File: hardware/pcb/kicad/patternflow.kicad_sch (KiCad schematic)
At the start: 11 parts, among them J1 Conn_02x08_Odd_Even, J3 Screw_Terminal_01x02, SW1 RotaryEncoder_Switch, SW2 RotaryEncoder_Switch, SW3 RotaryEncoder_Switch, SW4 RotaryEncoder_Switch, U1 ESP32-S3-DevKit-44pin

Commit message: hardware(pcb): v3.0 test board — hybrid power input (USB-C + 2-pin screw terminal)
Per the plan in issue #114: instead of splitting into two PCBs, one board now
carries both power-input options.

- Add a 2-pin screw terminal footprint on the back as a beginner-friendly
  bypass for the difficult USB-C THT soldering (strip a USB cable, screw it in)
- Clean up routing
- Bump silkscreen version text to v3.0
- Bake v3.0 test Gerbers (DRC clean: 0 violations, 0 unconnected) into
  hardware/pcb/gerber/experiment/ with a do-not-order README
- Delete patternflow_v2.2_test_gerber.zip so nobody orders the superseded
  test revision by mistake; BUILD_GUIDE warning updated to match

Co-Authored-By: Claude Opus 4.8 <noreply@anthropic.com>
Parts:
- added J4: Screw_Terminal_01x02, TerminalBlock:TerminalBlock_MaiXu_MX126-5.0-02P_1x02_P5.00mm, symbol Connector:Screw_Terminal_01x02
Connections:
- net +5V: now also J4.2 (Pin_2)
- net GND: now also J4.1 (Pin_1)
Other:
- title: PatternFlow -> Patternflow

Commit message: fix(pcb): correct C11 value typo 1000uF/1.6V -> 1000uF/16V
The part is a 16V Rubycon PX (16PX1000MEFC10X12.5); the schematic
value read 1.6V, which would be under-spec on the 5V rail.

Co-Authored-By: Claude Fable 5 <noreply@anthropic.com>
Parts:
- C11: value 1000uF/1.6V -> 1000uF/16V
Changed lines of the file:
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@@
 			)
 		)
-		(property "Value" "1000uF/1.6V"
+		(property "Value" "1000uF/16V"
 			(at 94.361 109.22 90)
 			(show_name no)

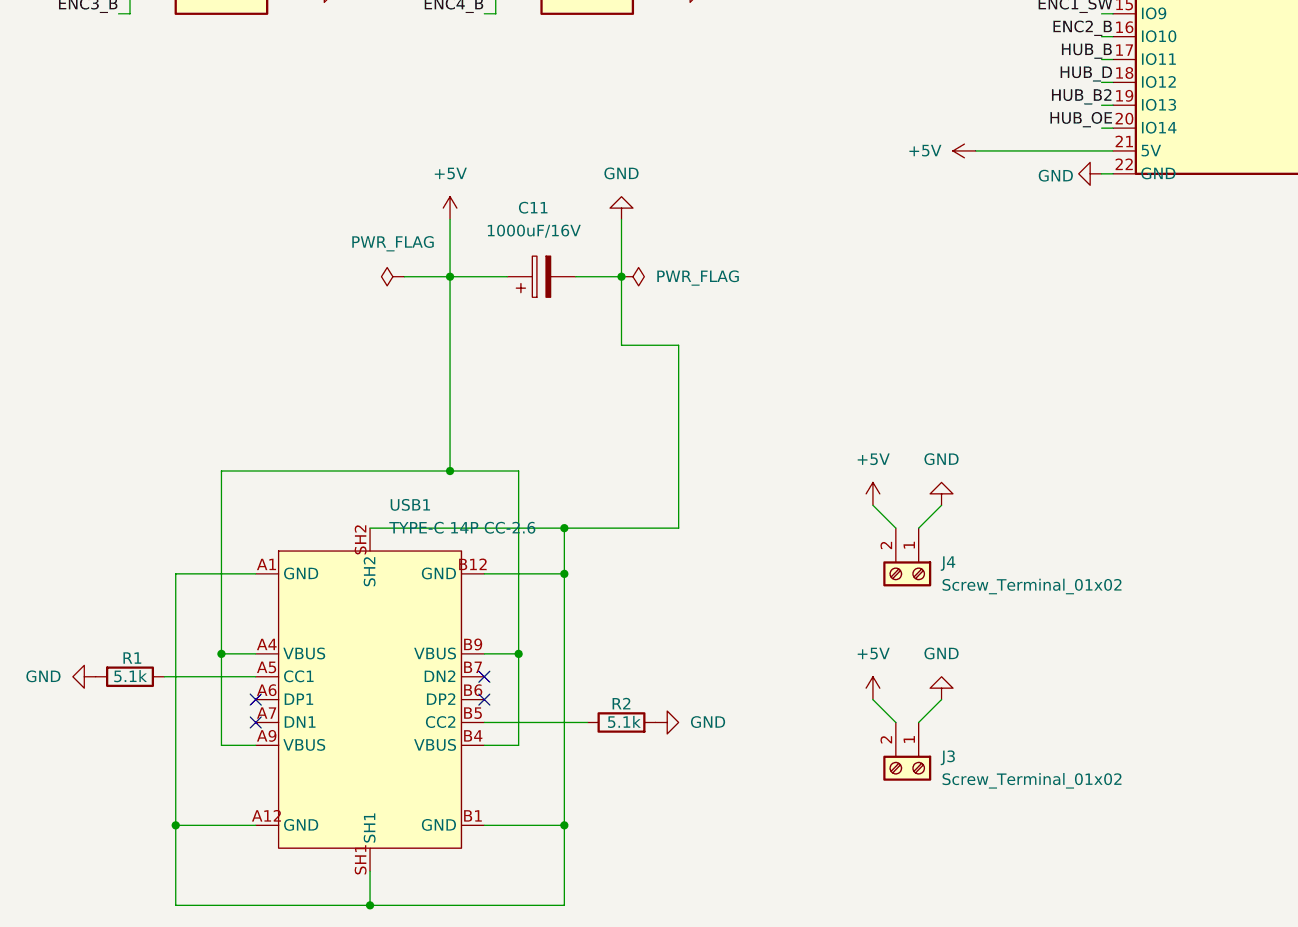
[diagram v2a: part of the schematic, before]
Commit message: hardware: v3.9 - the USB-C power input comes off the board, and the 330 case gets a wired route to the DevKit
v3.0 shipped a USB1 receptacle and its R1/R2 CC pull-downs that the build
guide, the BOM and the release notes all told you to leave unpopulated, after
the delayed burnout in #221. A footprint nobody is allowed to populate is an
instruction waiting to be ignored, so all three come off the board: J4, the
screw terminal, is the only power input there is.

Nothing else moved. The Edge_Cuts and NPTH gerbers are byte-identical to v3.0,
so the outline and every mounting hole are unchanged and the v3 cases fit both
boards. ERC went from 50 violations to 34 - the twelve pin_to_pin errors were
the USB-C net, and what remains are the same off-grid endpoints the fabricated
v3.0 carried. DRC reports no errors and no schematic-parity issues.

The 330 mm case gains a pass-through between the power-bank bay and the ESP32,
so a USB-C lead reaches the DevKit's own port with the case shut - for wired
features like MIDI and OSC, not for power - plus a cable exit slot below the
battery compartment. The 256 mm variant does not carry these yet.

Regenerated for v3.9: gerbers (14 files), BOM, board renders, schematic PDF and
SVG. The gerber command in the PCB README now pins the layer list, which is
what keeps the zip to the 14 fab files rather than all 29 layers.

Co-Authored-By: Claude Opus 5 <noreply@anthropic.com>
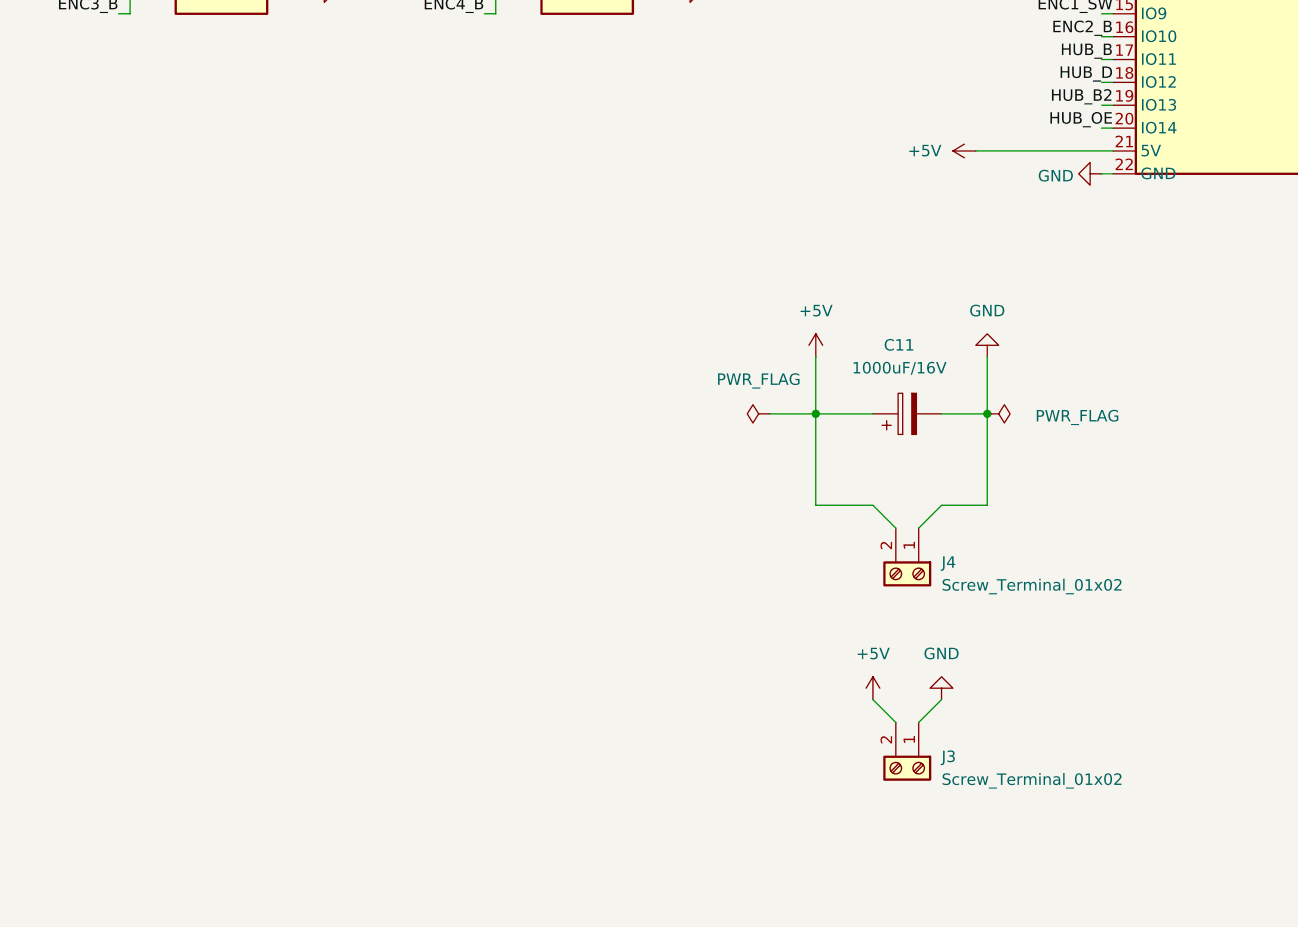
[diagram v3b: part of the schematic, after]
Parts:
- removed R1, R2: 5.1k, Resistor_THT:R_Axial_DIN0207_L6.3mm_D2.5mm_P7.62mm_Horizontal, symbol Device:R
- removed USB1: TYPE-C 14P CC-2.6, patternflow:TYPE-C-TH_TYPE-C-14P-CC-2.6, symbol patternflow:TYPE-C14PCC-2.6
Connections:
- no-connect marks 16 -> 12
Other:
- moved on the sheet: C11
